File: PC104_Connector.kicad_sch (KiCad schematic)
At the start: 2 parts

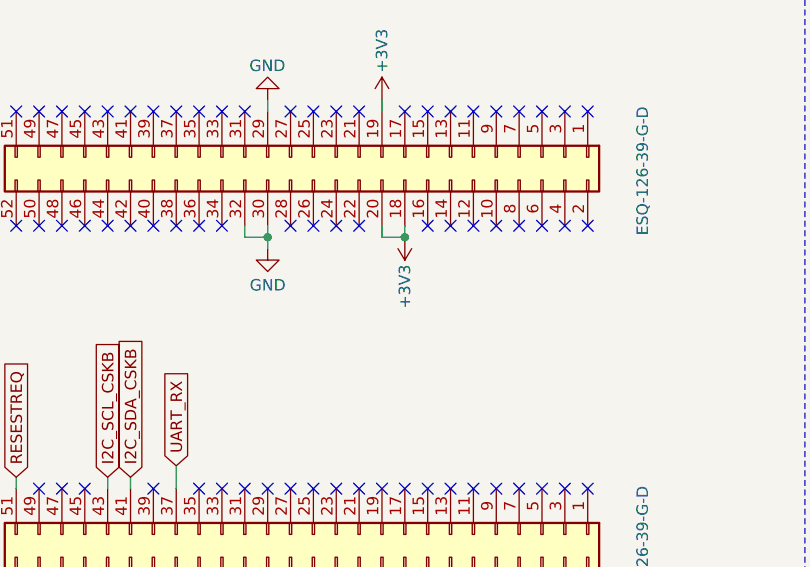
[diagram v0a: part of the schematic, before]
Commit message: Added some decoup caps and reviewed PCB layout
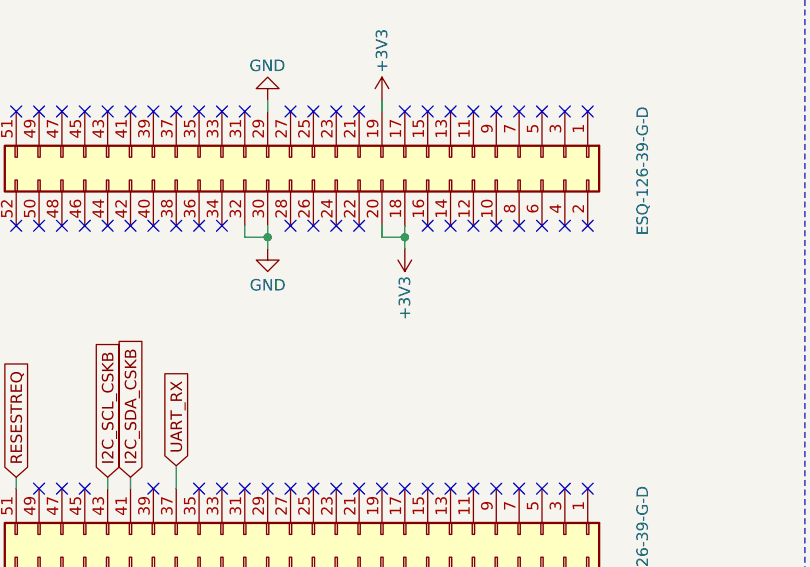
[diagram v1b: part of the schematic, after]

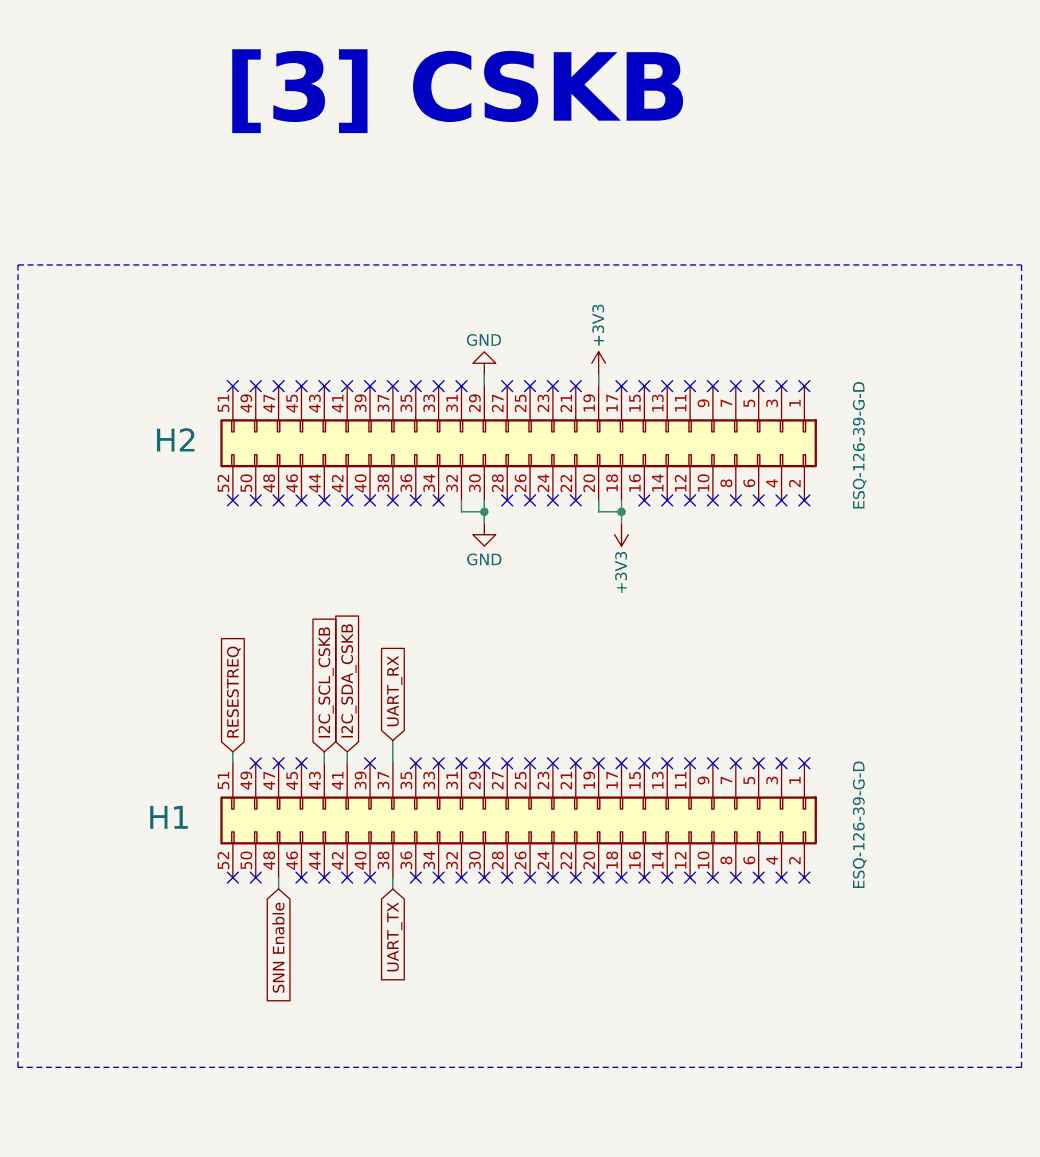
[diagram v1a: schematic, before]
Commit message: Added Level Shifter for SD card
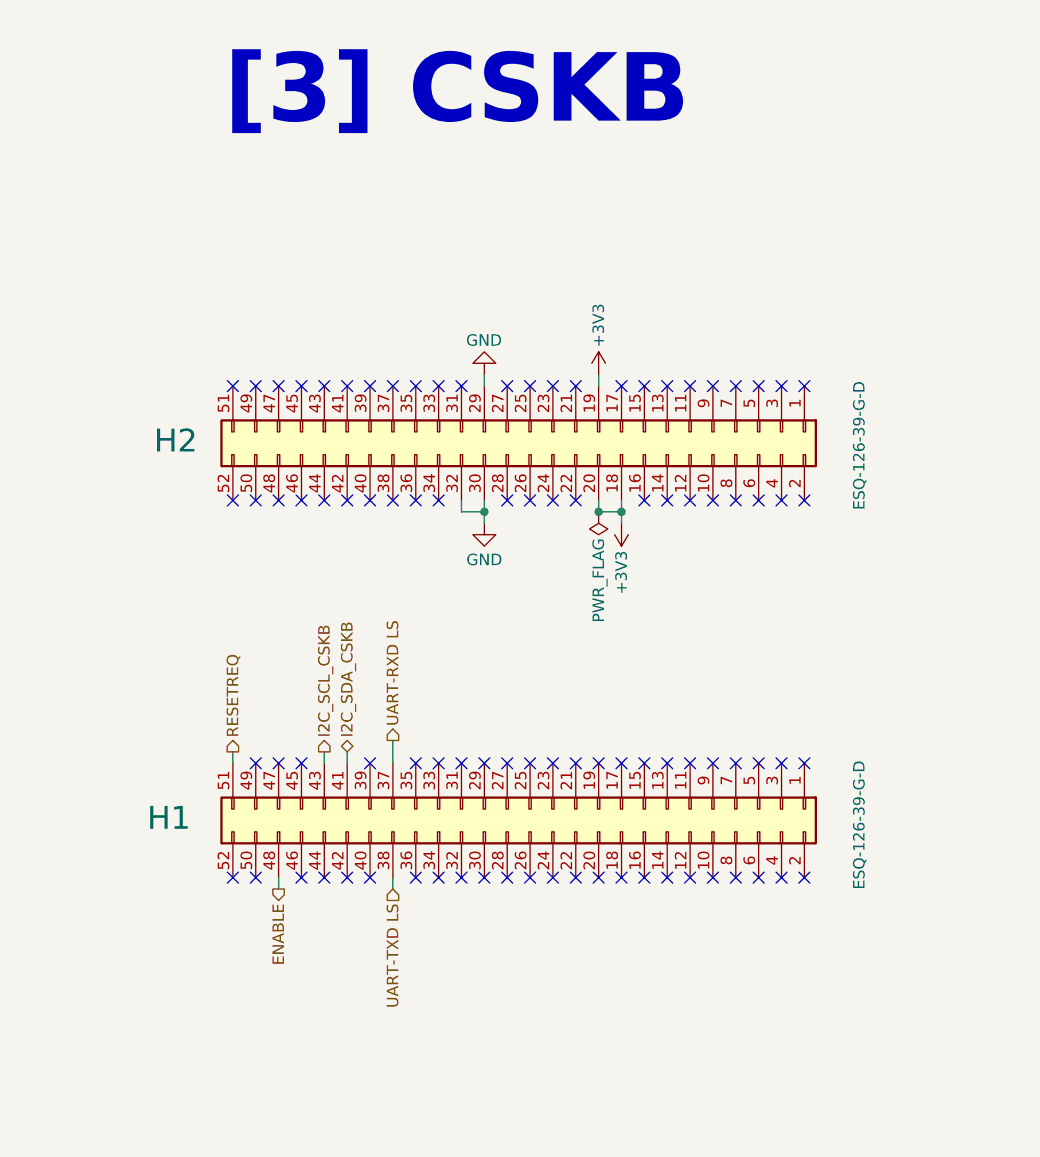
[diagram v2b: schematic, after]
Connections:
- net RESESTREQ renamed RESETREQ
- net SNN Enable renamed ENABLE
- net UART_RX renamed UART-RXD LS
- net UART_TX renamed UART-TXD LS
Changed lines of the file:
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@@
 	(generator_version "10.0")
 	(paper "A4")
-	(rectangle
-		(start 95.504 44.958)
-		(end 207.01 134.112)
-		(stroke
-			(width 0)
-			(type dash)
-		)
-		(fill
-			(type none)
-		)
-	)
 	(text "[3] CSKB"
 		(exclude_from_sim no)
@@
 		(color 0 0 0 0)
 	)
+	(junction
+		(at 160.02 72.39)
+		(diameter 0)
+		(color 0 0 0 0)
+	)
 	(no_connect
 		(at 142.24 58.42)
@@
 		)
 	)
-	(global_label "I2C_SCL_CSKB"
-		(shape input)
+	(hierarchical_label "I2C_SCL_CSKB"
+		(shape output)
 		(at 129.54 99.06 90)
-		(fields_autoplaced yes)
 		(effects
 			(font
@@
 			(justify left)
 		)
-		(property "Intersheetrefs" "${INTERSHEET_REFS}"
-			(at 129.54 82.5282 90)
-			(hide yes)
-			(show_name no)
-			(do_not_autoplace no)
-			(effects
-				(font
-					(size 1.27 1.27)
-				)
-				(justify left)
-			)
-		)
-	)
-	(global_label "I2C_SDA_CSKB"
-		(shape input)
-		(at 132.08 99.06 90)
-		(fields_autoplaced yes)
+	)
+	(hierarchical_label "UART-RXD LS"
+		(shape output)
+		(at 137.16 97.79 90)
 		(effects
 			(font
@@
 			(justify left)
 		)
-		(property "Intersheetrefs" "${INTERSHEET_REFS}"
-			(at 132.08 82.4677 90)
-			(hide yes)
-			(show_name no)
-			(do_not_autoplace no)
-			(effects
-				(font
-					(size 1.27 1.27)
-				)
-				(justify left)
-			)
-		)
-	)
-	(global_label "RESESTREQ"
-		(shape input)
-		(at 119.38 99.06 90)
-		(fields_autoplaced yes)
+	)
+	(hierarchical_label "I2C_SDA_CSKB"
+		(shape bidirectional)
+		(at 132.08 99.06 90)
 		(effects
 			(font
@@
 			(justify left)
 		)
-		(property "Intersheetrefs" "${INTERSHEET_REFS}"
-			(at 119.38 85.3707 90)
-			(hide yes)
-			(show_name no)
-			(do_not_autoplace no)
-			(effects
-				(font
-					(size 1.27 1.27)
-				)
-				(justify left)
-			)
-		)
-	)
-	(global_label "UART_RX"
+	)
+	(hierarchical_label "UART-TXD LS"
 		(shape input)
-		(at 137.16 97.79 90)
-		(fields_autoplaced yes)
+		(at 137.16 114.3 270)
 		(effects
 			(font
 				(size 1.27 1.27)
 			)
-			(justify left)
-		)
-		(property "Intersheetrefs" "${INTERSHEET_REFS}"
-			(at 137.16 86.701 90)
-			(hide yes)
-			(show_name no)
-			(do_not_autoplace no)
-			(effects
-				(font
-					(size 1.27 1.27)
-				)
-				(justify left)
-			)
-		)
-	)
-	(global_label "UART_TX"
-		(shape input)
-		(at 137.16 114.3 270)
-		(fields_autoplaced yes)
+			(justify right)
+		)
+	)
+	(hierarchical_label "RESETREQ"
+		(shape output)
+		(at 119.38 99.06 90)
 		(effects
 			(font
 				(size 1.27 1.27)
 			)
-			(justify right)
-		)
-		(property "Intersheetrefs" "${INTERSHEET_REFS}"
-			(at 137.16 125.0866 90)
-			(hide yes)
-			(show_name no)
-			(do_not_autoplace no)
-			(effects
-				(font
-					(size 1.27 1.27)
-				)
-				(justify right)
-			)
-		)
-	)
-	(global_label "SNN Enable"
-		(shape input)
+			(justify left)
+		)
+	)
+	(hierarchical_label "ENABLE"
+		(shape output)
 		(at 124.46 114.3 270)
-		(fields_autoplaced yes)
 		(effects
 			(font
@@
 			)
 			(justify right)
-		)
-		(property "Intersheetrefs" "${INTERSHEET_REFS}"
-			(at 124.46 128.4731 90)
-			(hide yes)
-			(show_name no)
-			(do_not_autoplace no)
-			(effects
-				(font
-					(size 1.27 1.27)
-				)
-				(justify right)
-			)
 		)
 	)
@@
 					(unit 1)
 				)
+			)
+		)
+	)
+	(symbol
+		(lib_id "power:PWR_FLAG")
+		(at 160.02 72.39 180)
+		(unit 1)
+		(body_style 1)
+		(exclude_from_sim no)
+		(in_bom yes)
+		(on_board yes)
+		(in_pos_files yes)
+		(dnp no)
+		(property "Reference" "#FLG01"
+			(at 160.02 74.295 0)
+			(hide yes)
+			(show_name no)
+			(do_not_autoplace no)
+			(effects
+				(font
+					(size 1.27 1.27)
+				)
+			)
+		)
+		(property "Value" "PWR_FLAG"
+			(at 160.02 80.01 90)
+			(show_name no)
+			(do_not_autoplace no)
+			(effects
+				(font
+					(size 1.27 1.27)
+				)
+			)
+		)
+		(property "Footprint" ""
+			(at 160.02 72.39 0)
+			(hide yes)
+			(show_name no)
+			(do_not_autoplace no)
+			(effects
+				(font
+					(size 1.27 1.27)
+				)
+			)
+		)
+		(property "Datasheet" ""
+			(at 160.02 72.39 0)
+			(hide yes)
+			(show_name no)
+			(do_not_autoplace no)
+			(effects
+				(font
+					(size 1.27 1.27)
+				)
+			)
+		)
+		(property "Description" "Special symbol for telling ERC where power comes from"
+			(at 160.02 72.39 0)
+			(hide yes)
+			(show_name no)
+			(do_not_autoplace no)
+			(effects
+				(font
+					(size 1.27 1.27)
+				)
+			)
+		)
+		(pin "1"
+		)
+		(instances
+			(project "adapter-pcb"
+				(path "/94da9b83-1146-4f01-8e34-8153765b0257/6da06bd5-7839-43dd-9065-41aec0431e8e"
+					(reference "#FLG01")
+					(unit 1)
+				)

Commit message: Added pcb files for ethernet breakout board
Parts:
- H1, H2: MANUFACTURER SAMTEC -> Samtec; MPN (none) -> C7466599
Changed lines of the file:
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@@
 			)
 		)
-		(property "MANUFACTURER" "SAMTEC"
+		(property "MANUFACTURER" "Samtec"
 			(at 152.4 105.41 90)
 			(hide yes)
@@
 		)
 		(property "MANUFACTURER_PART_NUMBER" "ESQ-126-39-G-D"
+			(at 152.4 105.41 90)
+			(hide yes)
+			(show_name no)
+			(do_not_autoplace no)
+			(effects
+				(font
+					(size 1.27 1.27)
+				)
+			)
+		)
+		(property "External Part Number" ""
+			(at 152.4 105.41 90)
+			(hide yes)
+			(show_name no)
+			(do_not_autoplace no)
+			(effects
+				(font
+					(size 1.27 1.27)
+				)
+			)
+		)
+		(property "MPN" "C7466599"
 			(at 152.4 105.41 90)
 			(hide yes)
@@
 			)
 		)
-		(property "MANUFACTURER" "SAMTEC"
+		(property "MANUFACTURER" "Samtec"
 			(at 152.4 63.5 90)
 			(hide yes)
@@
 			(at 152.4 63.5 90)
 			(hide yes)
+			(show_name no)
+			(do_not_autoplace no)
+			(effects
+				(font
+					(size 1.27 1.27)
+				)
+			)
+		)
+		(property "External Part Number" ""
+			(at 152.4 63.5 90)
+			(hide yes)
+			(show_name no)
+			(do_not_autoplace no)
+			(effects
+				(font
+					(size 1.27 1.27)
+				)
+			)
+		)
+		(property "MPN" "C7466599"
+			(at 152.4 63.5 90)
+			(hide yes)

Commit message: Updated BOM and added fiducials
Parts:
- H1, H2: External Part Number (none) -> ESQ-126-39-G-D; MANUFACTURER_PART_NUMBER ESQ-126-39-G-D -> (none)
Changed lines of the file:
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@@
 			)
 		)
-		(property "MANUFACTURER_PART_NUMBER" "ESQ-126-39-G-D"
-			(at 152.4 105.41 90)
-			(hide yes)
-			(show_name no)
-			(do_not_autoplace no)
-			(effects
-				(font
-					(size 1.27 1.27)
-				)
-			)
-		)
-		(property "External Part Number" ""
+		(property "External Part Number" "ESQ-126-39-G-D"
 			(at 152.4 105.41 90)
 			(hide yes)
@@
 			)
 		)
-		(property "MANUFACTURER_PART_NUMBER" "ESQ-126-39-G-D"
+		(property "External Part Number" "ESQ-126-39-G-D"
 			(at 152.4 63.5 90)
 			(hide yes)
-			(show_name no)
-			(do_not_autoplace no)
-			(effects
-				(font
-					(size 1.27 1.27)
-				)
-			)
-		)
-		(property "External Part Number" ""
-			(at 152.4 63.5 90)
-			(hide yes)
